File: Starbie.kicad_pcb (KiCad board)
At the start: 2 copper layers, 96.6 x 82.8 mm, 7 parts, among them J1 OLED, J2 MPU6050, SW1 SW_Push, SW2 SW_Push, U1 DHT11, U2 XIAO-ESP32-C3-SMD

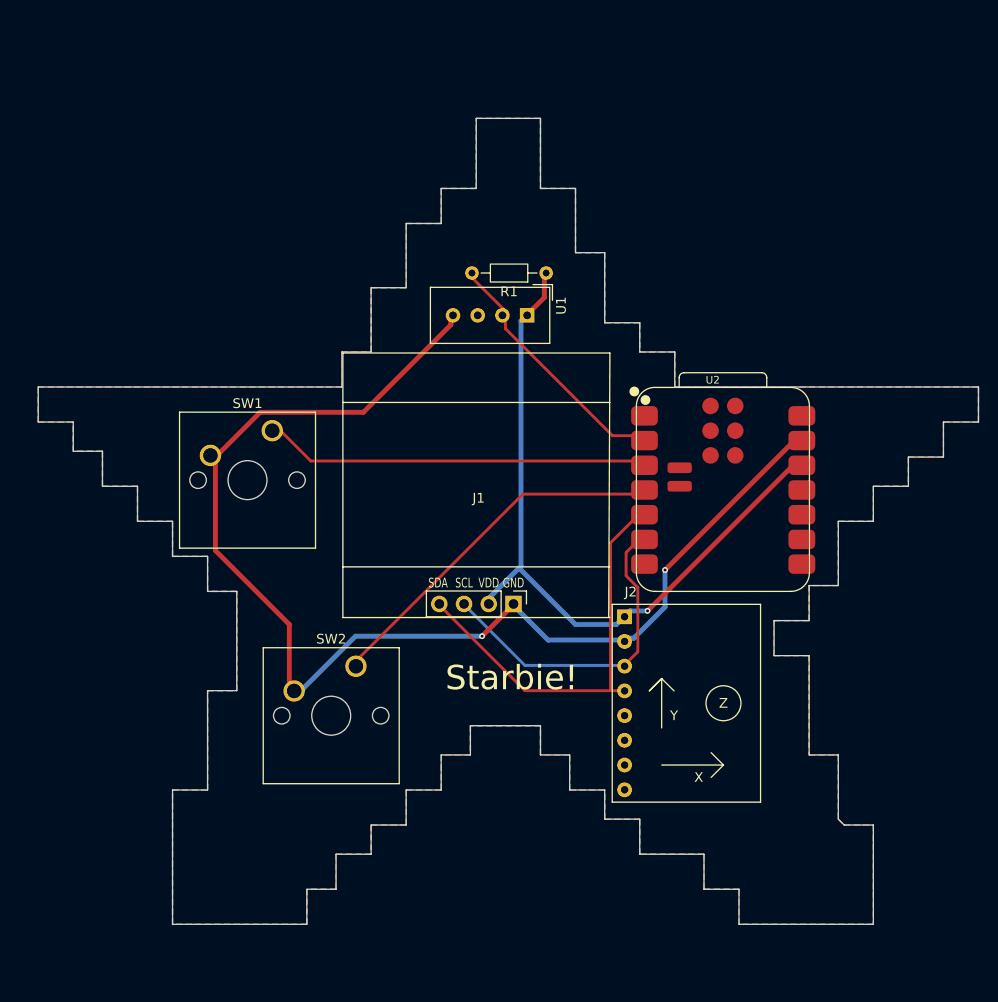
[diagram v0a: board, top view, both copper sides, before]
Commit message: Feat: Redesign to make jet shaped outline + add BOM and CPL files
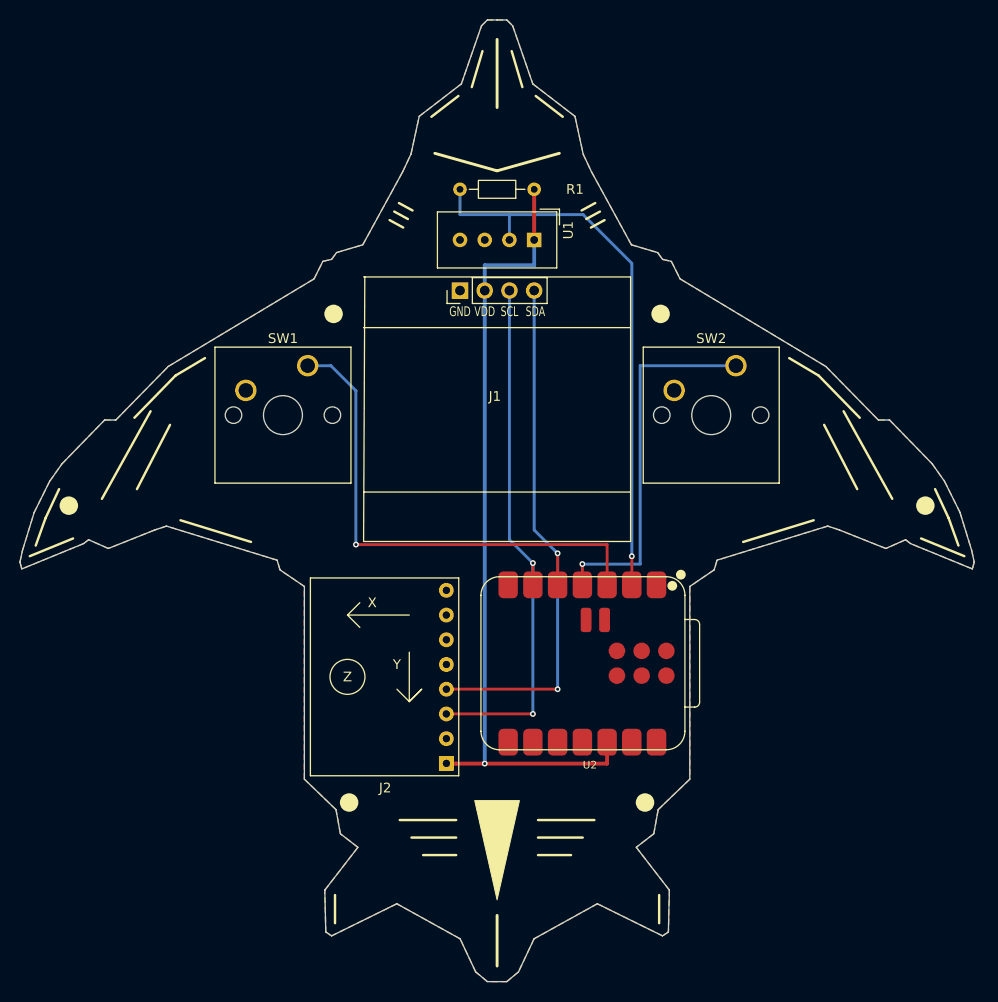
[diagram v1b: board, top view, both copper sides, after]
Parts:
- moved SW2 49.8 mm to (142.0, 55.9)
- moved J1 32.3 mm to (117.5, 48.2), turned to 0 degrees
- moved J2 23.7 mm to (112.3, 96.8), turned to 180 degrees
- moved U2 16.1 mm to (115.8, 77.6), turned to -90 degrees
- moved R1 8.69 mm to (121.3, 37.8)
- moved U1 7.78 mm to (121.3, 43.0)
- moved SW1 7.61 mm to (98.0, 55.9)
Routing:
- net GND: track 126.9 -> 0.00 mm, vias 2 -> 0
- net /DHT11_DATA: track 26.1 -> 58.0 mm, vias 0 -> 1
- net /SCL: track 34.2 -> 55.6 mm, vias 0 -> 2
- net /SDA: track 42.5 -> 56.6 mm, vias 0 -> 2
- net /BUTTON1: track 39.6 -> 51.8 mm, vias 0 -> 1
- net +3V3: track 74.5 -> 82.8 mm
- net /BUTTON2: track 37.3 -> 38.3 mm, vias 0 -> 1
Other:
- board size 96.6 x 82.8 mm -> 98 x 98.8 mm
